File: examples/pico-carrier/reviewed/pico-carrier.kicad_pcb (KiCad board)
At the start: 2 copper layers, 88 x 62 mm, 9 parts, among them J1 5V IN, J3 GP0-GP15, J4 GP16-GP28, PWR, U1 Pico

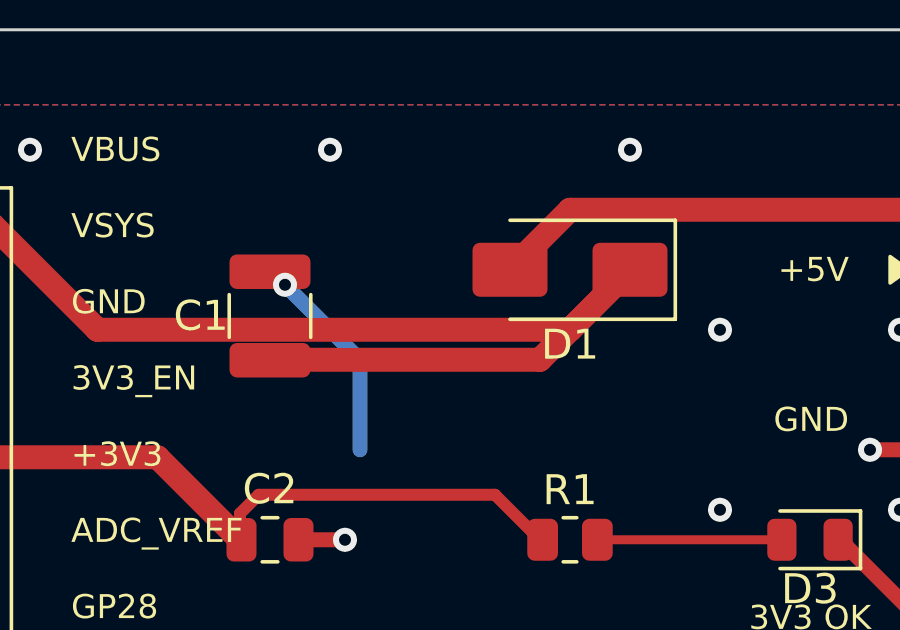
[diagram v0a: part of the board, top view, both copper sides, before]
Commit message: Stop hiding the hairpins behind the pads they are drawn on
The reviewer said the 135 degree bends and the odd-angle runs were still
there. They were. `route.acute_angle` skipped any corner within a pad's
*radius*, and a 0805's radius is 0.47 mm, which covers the five or six
ordinary corners a chamfered pad entry leaves inside it. Eleven of the
thirteen hairpins on these five boards sat in that shadow, because a pad
is exactly where a route that has to double back does it.

The exemption is the pad's connection point now, not a disc around it.
Two branches leaving one pad stay exempt - the pad's own copper fills the
wedge, so it is not an acid trap - but nought degrees never is: that is
one run drawn twice, and no pad excuses it.

Then the generator had to stop making them:

* `_untraced` drops the copper a second run lays on top of the first.
  The shorter is inside the longer and carries nothing it does not; both
  get trimmed, because dropping only the duplicate leaves the other
  hanging over the gap, which is `route.stub`. It runs before the runs
  are joined, while the pair is still two tracks sharing an end - once
  joined, the shared point is usually a pad, and the clean-up passes pin
  those precisely so they cannot take copper off them.
* `_straighten` only takes the direct line when it lands on the 45 grid.
  Between two pads at whatever coordinates their packages give them it
  usually does not: last round it made a nine millimetre run at 169.7
  degrees, which is the slip-of-the-mouse angle `route.odd_angle` is for.

Measured across the five boards: off-grid segments 1 to 0, 180 degree
reversals 6 to 0, and the motor board's `route.return_path` finding went
with the 11 mm of copper it was measuring.

Three corners survive, all on the FPGA board, all where a knee lands a
fraction past where its own two legs cross - legs of 0.07 and 0.25 mm on
two, 0.15 and 0.5 mm on the third. Refusing a knee that short is worse:
the segment then keeps the angle it had, a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
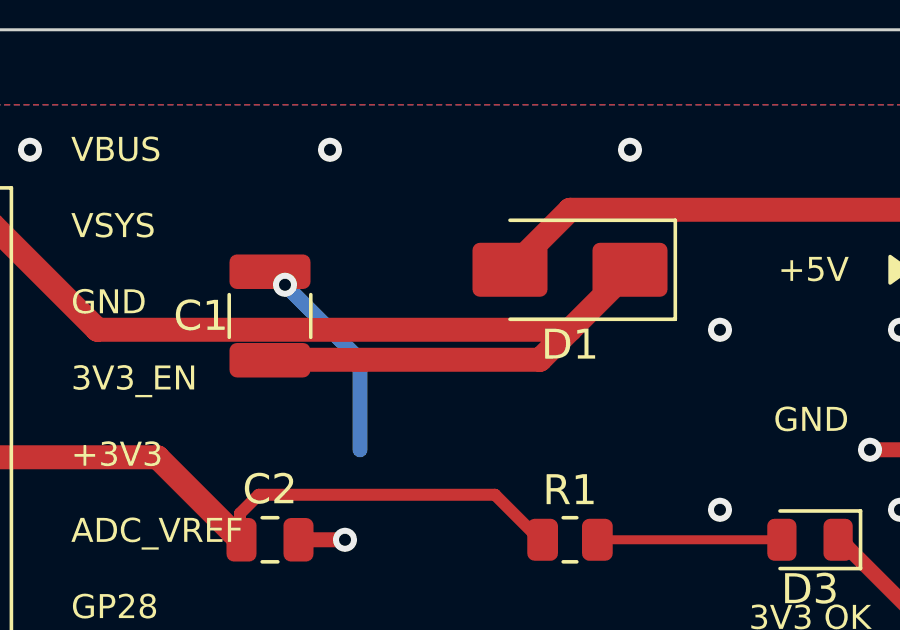
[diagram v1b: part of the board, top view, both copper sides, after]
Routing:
- net /VSYS: track 43.9 -> 41.0 mm
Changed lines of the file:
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@@
 	(segment (start 142.75 66.5) (end 146.25 70.0) (width 0.8) (layer "F.Cu") (net 36))
 	(segment (start 146.25 70.0) (end 162.0 70.0) (width 0.8) (layer "F.Cu") (net 36))
-	(segment (start 162.0 70.0) (end 164.0 68.0) (width 0.8) (layer "F.Cu") (net 36))
-	(segment (start 164.0 68.0) (end 161.0 71.0) (width 0.8) (layer "F.Cu") (net 36))
-	(segment (start 161.0 71.0) (end 152.25 71.0) (width 0.8) (layer "F.Cu") (net 36))
-	(segment (start 152.25 71.0) (end 152.235 71.015) (width 0.8) (layer "F.Cu") (net 36))
-	(segment (start 152.235 71.015) (end 152.0 71.015) (width 0.8) (layer "F.Cu") (net 36))
 	(segment (start 135.69 69.08) (end 142.0 69.08) (width 0.8) (layer "F.Cu") (net 1))
 	(segment (start 135.69 71.62) (end 142.0 71.62) (width 0.3) (layer "F.Cu") (net 4))
@@
 	(segment (start 176.0 66.0) (end 162.0 66.0) (width 0.8) (layer "F.Cu") (net 3))
 	(segment (start 162.0 66.0) (end 160.0 68.0) (width 0.8) (layer "F.Cu") (net 3))
+	(segment (start 152.0 71.015) (end 152.235 71.015) (width 0.8) (layer "F.Cu") (net 36))
+	(segment (start 152.235 71.015) (end 152.25 71.0) (width 0.8) (layer "F.Cu") (net 36))
+	(segment (start 152.25 71.0) (end 161.0 71.0) (width 0.8) (layer "F.Cu") (net 36))
+	(segment (start 161.0 71.0) (end 164.0 68.0) (width 0.8) (layer "F.Cu") (net 36))
 	(segment (start 151.05 77.0) (end 151.05 76.8) (width 0.4) (layer "F.Cu") (net 2))
 	(segment (start 151.05 76.8) (end 151.0 76.75) (width 0.4) (layer "F.Cu") (net 2))

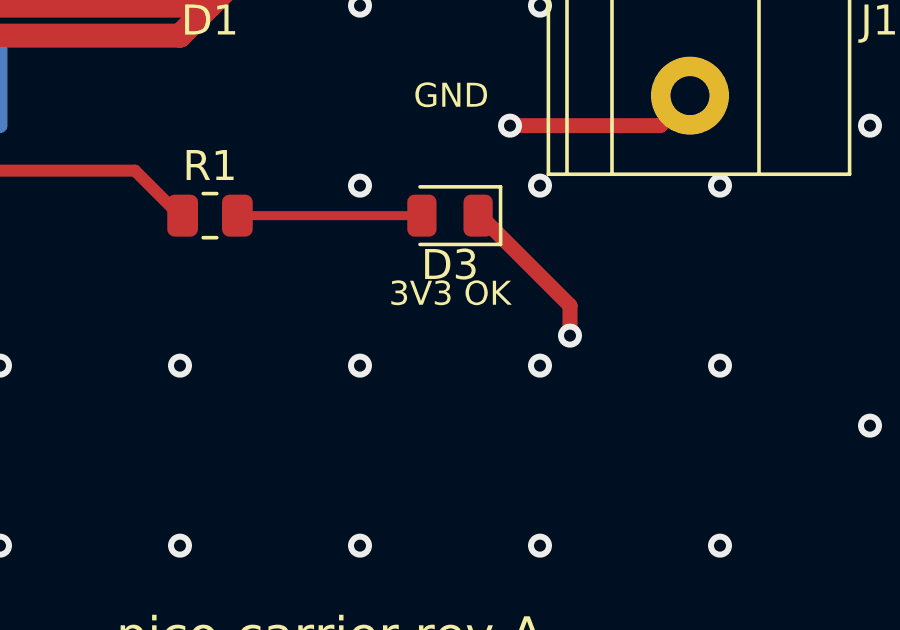
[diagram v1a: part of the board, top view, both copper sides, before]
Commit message: Rip up copper that tours, and put a footprint's zones where the footprint is
The plots showed three things on the artwork side that no rule reported.

**A track that goes round the board to cover thirteen millimetres.** The
op-amp's feedback wrap had to get from one side of a SOT-23-5 to the other
and, routed last, took fifty-six millimetres of tour because everything
nearer was already spoken for. That is an ordering problem, so the loop that
fixes ordering fixes it: `_route_all` now reports what each track cost
against `route.wander`'s own baseline - imported, not copied, so the two
cannot drift - and the worst tour goes to the front and the set is routed
again. A track that still tours from first pick has nowhere better to be and
is left alone. The default order is shortest-first for the same reason: a
thirteen millimetre connection has few ways to be made and a forty
millimetre one has many. The learned order is now written on every change,
not only on success, because an afternoon of rip-ups is worth keeping when
the machine goes away in the middle.

**A keep-out sitting at the origin.** A footprint may carry zones of its own
and KiCad stores *those* in board coordinates while everything else in a
footprint is stored relative to it. The Pico module's two pad keep-outs had
been at (0, -6) for four rounds - off the board, keeping nothing out. DRC is
silent because an empty region violates no rule, and the only visible sign
was the plot: "fit to page" fits the bounding box, so every view of that
board came out at half scale in one corner with the rest blank.
`layout.zone_outside_outline` reports it; the placer moves it.

**Silkscreen printed through silkscreen.** The schematic has
`readability.text_over_text` and the board had nothing, though the board is
the harder case - a sheet can be zoomed and a bare board cannot.
`silk.text_over_text` measures it from the font size the file states; on
KiCad's demo boards it fires on 6 of 16, 173 times. The generator places t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
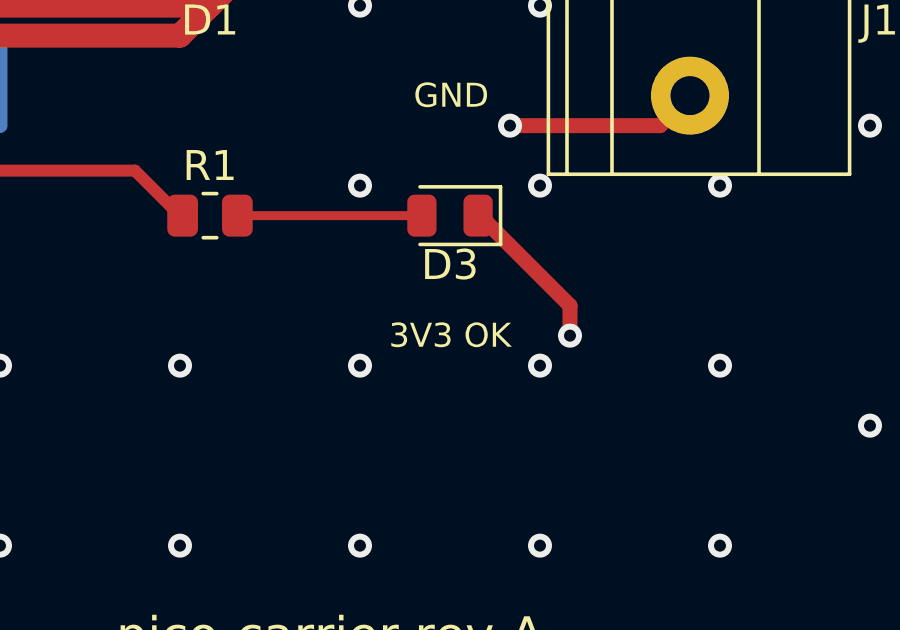
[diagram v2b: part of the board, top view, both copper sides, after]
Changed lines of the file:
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@@
       (polygon
         (pts
-          (xy 0.052139 -5.515545)
-          (xy 0.086068 -5.642167)
-          (xy 0.151612 -5.755694)
-          (xy 0.244306 -5.848388)
-          (xy 0.357833 -5.913932)
-          (xy 0.484455 -5.947861)
-          (xy 0.55 -5.95)
-          (xy 1 -5.95)
-          (xy 1 -4.05)
-          (xy 0.55 -4.05)
-          (xy 0.484455 -4.052139)
-          (xy 0.357833 -4.086068)
-          (xy 0.244306 -4.151612)
-          (xy 0.151612 -4.244306)
-          (xy 0.086068 -4.357833)
-          (xy 0.052139 -4.484455)
-          (xy 0.05 -4.55)
-          (xy 0.05 -5.45)
+          (xy 126.052139 82.614455)
+          (xy 126.086068 82.487833)
+          (xy 126.151612 82.374306)
+          (xy 126.244306 82.281612)
+          (xy 126.357833 82.216068)
+          (xy 126.484455 82.182139)
+          (xy 126.55 82.18)
+          (xy 127.0 82.18)
+          (xy 127.0 84.08)
+          (xy 126.55 84.08)
+          (xy 126.484455 84.077861)
+          (xy 126.357833 84.043932)
+          (xy 126.244306 83.978388)
+          (xy 126.151612 83.885694)
+          (xy 126.086068 83.772167)
+          (xy 126.052139 83.645545)
+          (xy 126.05 83.58)
+          (xy 126.05 82.68)
         )
       )
@@
       (polygon
         (pts
-          (xy 1 -4.05)
-          (xy 1.45 -4.05)
-          (xy 1.515545 -4.052139)
-          (xy 1.642167 -4.086067)
-          (xy 1.755694 -4.151612)
-          (xy 1.848388 -4.244306)
-          (xy 1.913933 -4.357833)
-          (xy 1.947861 -4.484455)
-          (xy 1.95 -4.55)
-          (xy 1.95 -5.45)
-          (xy 1.947861 -5.515545)
-          (xy 1.913933 -5.642167)
-          (xy 1.848388 -5.755694)
-          (xy 1.755694 -5.848388)
-          (xy 1.642167 -5.913933)
-          (xy 1.515545 -5.947861)
-          (xy 1.45 -5.95)
-          (xy 1 -5.95)
+          (xy 127.0 84.08)
+          (xy 127.45 84.08)
+          (xy 127.515545 84.077861)
+          (xy 127.642167 84.043933)
+          (xy 127.755694 83.978388)
+          (xy 127.848388 83.885694)
+          (xy 127.913933 83.772167)
+          (xy 127.947861 83.645545)
+          (xy 127.95 83.58)
+          (xy 127.95 82.68)
+          (xy 127.947861 82.614455)
+          (xy 127.913933 82.487833)
+          (xy 127.848388 82.374306)
+          (xy 127.755694 82.281612)
+          (xy 127.642167 82.216067)
+          (xy 127.515545 82.182139)
+          (xy 127.45 82.18)
+          (xy 127.0 82.18)
         )
       )
@@
 	(gr_text "+5V" (at 171.3 68.0 0) (layer "F.SilkS") (effects (font (size 0.8 0.8) (thickness 0.12)) (justify right)))
 	(gr_text "GND" (at 171.3 73.0 0) (layer "F.SilkS") (effects (font (size 0.8 0.8) (thickness 0.12)) (justify right)))
-	(gr_text "3V3 OK" (at 170.0 79.6 0) (layer "F.SilkS") (effects (font (size 0.8 0.8) (thickness 0.12))))
+	(gr_text "3V3 OK" (at 170.0 81.0 0) (layer "F.SilkS") (effects (font (size 0.8 0.8) (thickness 0.12))))
 )
